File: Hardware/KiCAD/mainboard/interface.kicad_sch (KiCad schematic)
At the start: 25 parts, among them J2 USB_C, J3 Conn_01x04, J4 Conn_01x24, J5 STLink, Q1 BSS138, U5 USBLC6-2

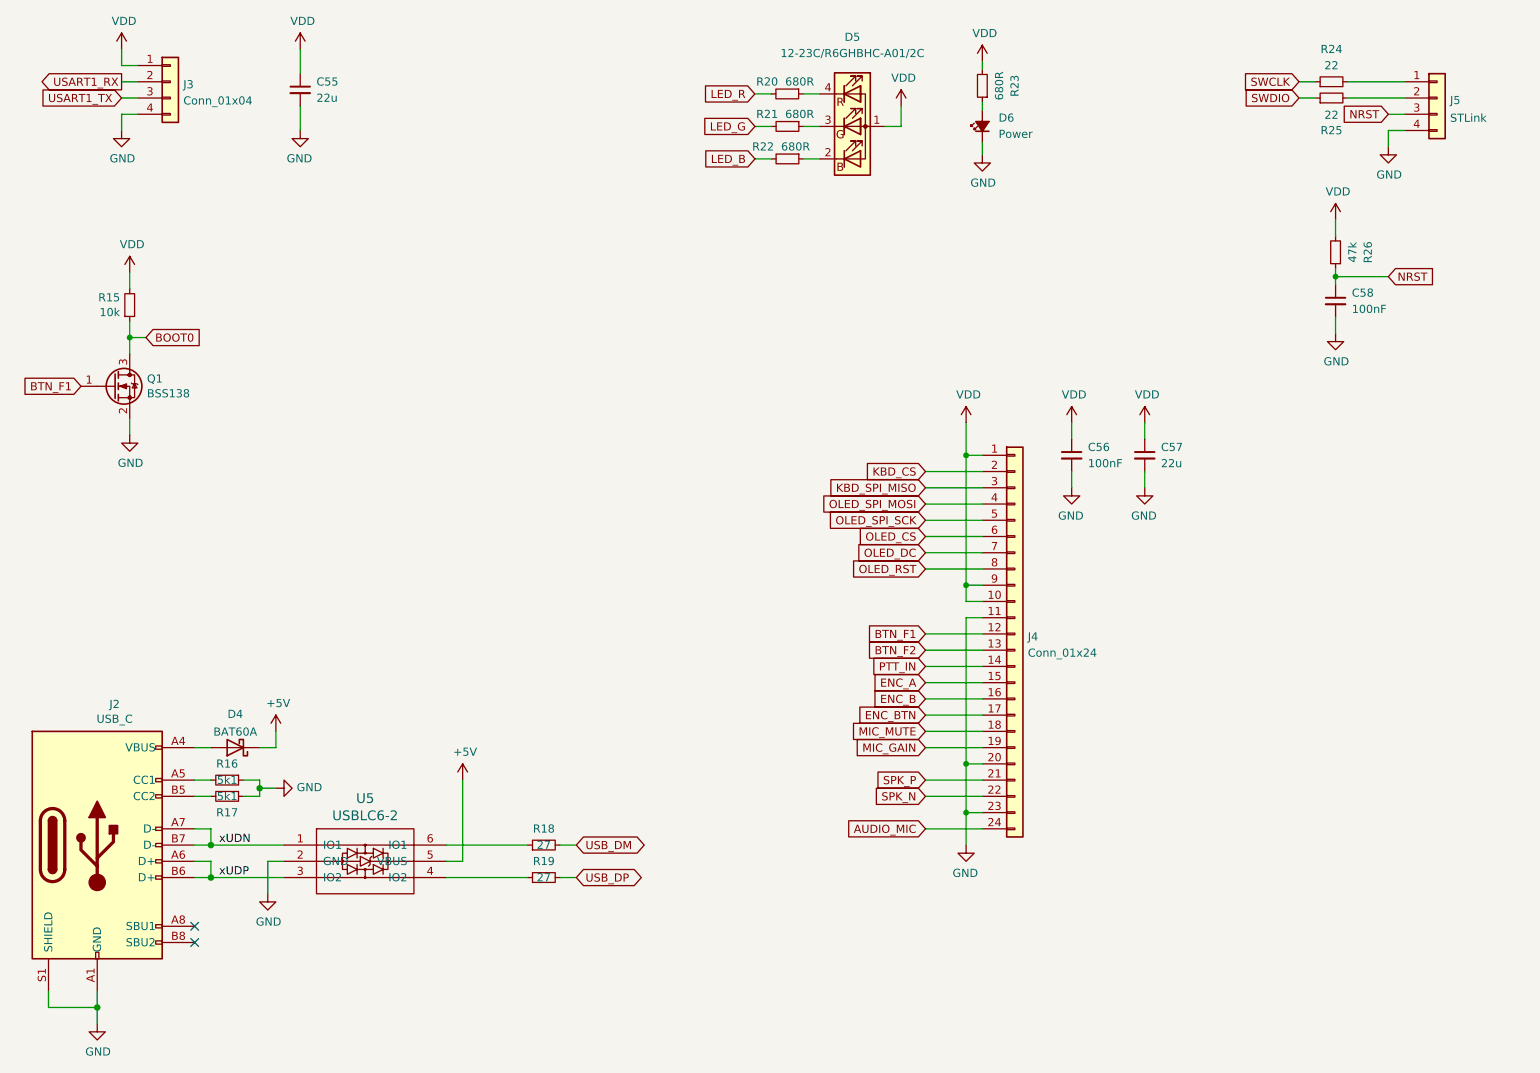
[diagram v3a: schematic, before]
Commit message: Removed RTC
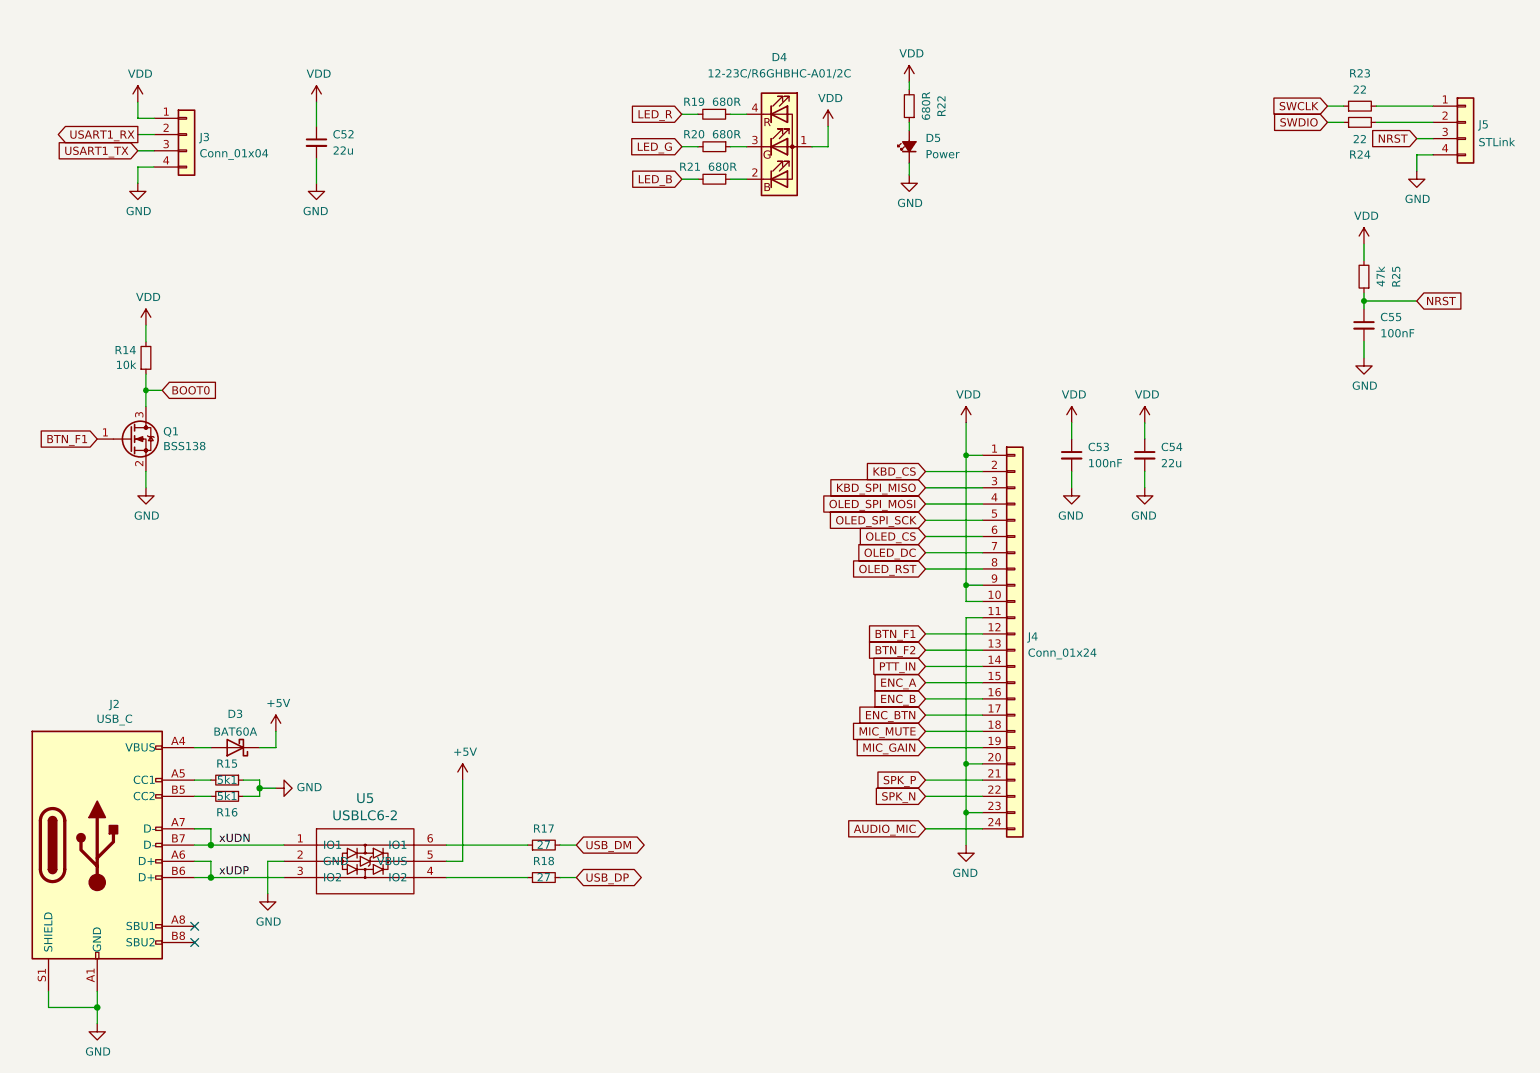
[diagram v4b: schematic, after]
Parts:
- J4: footprint (none) -> Connector_FFC-FPC:Hirose_FH12-24S-0.5SH_1x24-1MP_P0.50mm_Horizontal
- renumbered C55 to C52, C56 to C53, C57 to C54, C58 to C55, D4 to D3, D5 to D4, D6 to D5, R15 to R14, R16 to R15, R17 to R16, R18 to R17, R19 to R18, R20 to R19, R21 to R20, R22 to R21, R23 to R22, R24 to R23, R25 to R24, R26 to R25
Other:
- moved on the sheet: C52, C55, D4, D5, J3, J5, Q1, R14, R19, R20, R21, R22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

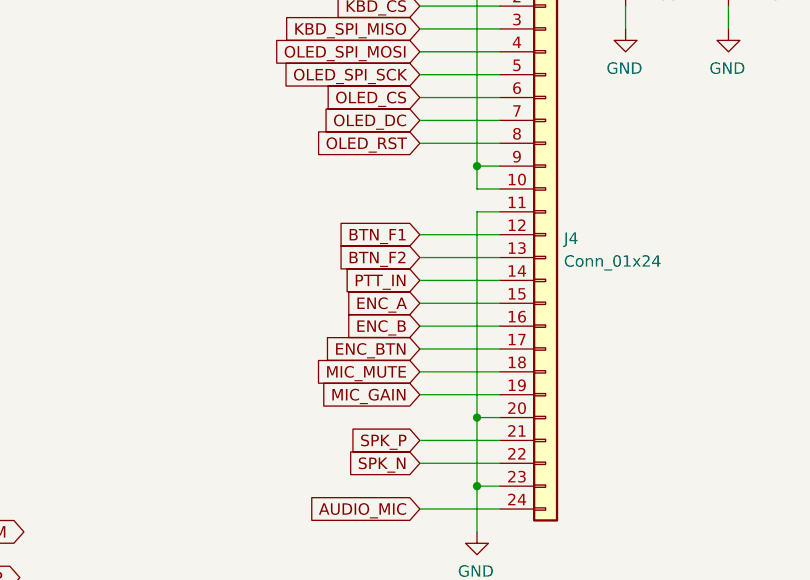
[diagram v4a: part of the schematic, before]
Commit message: Add ANY_KEY signal from keypad.
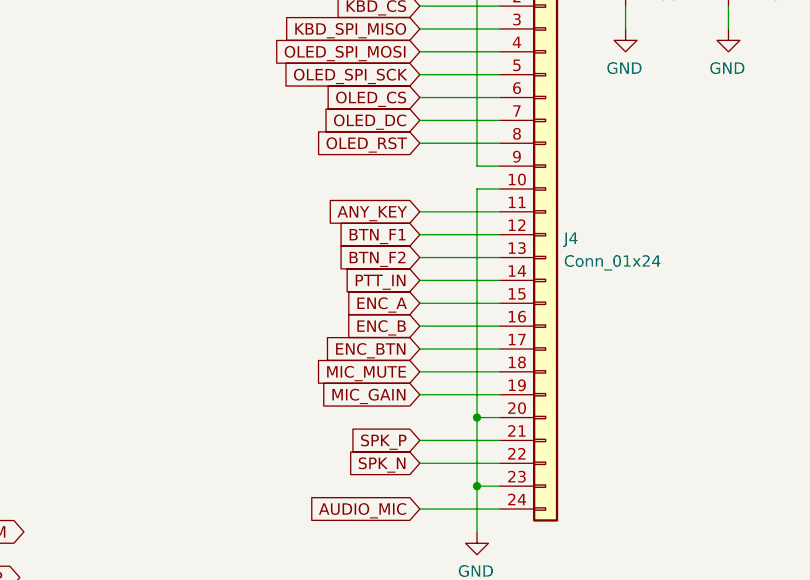
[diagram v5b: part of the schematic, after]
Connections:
- net GND: now also J4.10 (Pin_10); no longer J4.11 (Pin_11)
- net VDD: no longer J4.10 (Pin_10)
- new net ANY_KEY: J4.11 (Pin_11)
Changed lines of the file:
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@@
   (junction (at 44.45 83.82) (diameter 0) (color 0 0 0 0)
-  )
-  (junction (at 172.72 114.3) (diameter 0) (color 0 0 0 0)
   )
   (junction (at 172.72 142.24) (diameter 0) (color 0 0 0 0)
@@
     (stroke (width 0) (type default) (color 0 0 0 0))
   )
-  (wire (pts (xy 172.72 116.84) (xy 172.72 114.3))
-    (stroke (width 0) (type default) (color 0 0 0 0))
-  )
   (wire (pts (xy 166.37 96.52) (xy 175.26 96.52))
     (stroke (width 0) (type default) (color 0 0 0 0))
@@
     (stroke (width 0) (type default) (color 0 0 0 0))
   )
-  (wire (pts (xy 175.26 119.38) (xy 172.72 119.38))
-    (stroke (width 0) (type default) (color 0 0 0 0))
-  )
   (wire (pts (xy 54.61 152.4) (xy 54.61 154.94))
     (stroke (width 0) (type solid) (color 0 0 0 0))
@@
     (stroke (width 0) (type solid) (color 0 0 0 0))
   )
+  (wire (pts (xy 166.37 119.38) (xy 175.26 119.38))
+    (stroke (width 0) (type default) (color 0 0 0 0))
+  )
   (wire (pts (xy 166.37 139.7) (xy 175.26 139.7))
     (stroke (width 0) (type default) (color 0 0 0 0))
@@
     (stroke (width 0) (type solid) (color 0 0 0 0))
   )
-  (wire (pts (xy 172.72 119.38) (xy 172.72 142.24))
+  (wire (pts (xy 172.72 116.84) (xy 172.72 142.24))
     (stroke (width 0) (type default) (color 0 0 0 0))
   )
@@
       (effects (font (size 1.27 1.27)) (justify right) hide)
     )
+  )
+  (global_label "ANY_KEY" (shape input) (at 166.37 119.38 180) (fields_autoplaced)
+    (effects (font (size 1.27 1.27)) (justify right))
+    (property "Intersheet References" "${INTERSHEET_REFS}" (id 0) (at 155.974 119.3006 0)
+      (effects (font (size 1.27 1.27)) (justify right) hide)
+    )
